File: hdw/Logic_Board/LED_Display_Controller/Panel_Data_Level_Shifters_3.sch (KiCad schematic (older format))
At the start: 43 parts, among them U2801 74LVC1G32, U2802 74HCT541

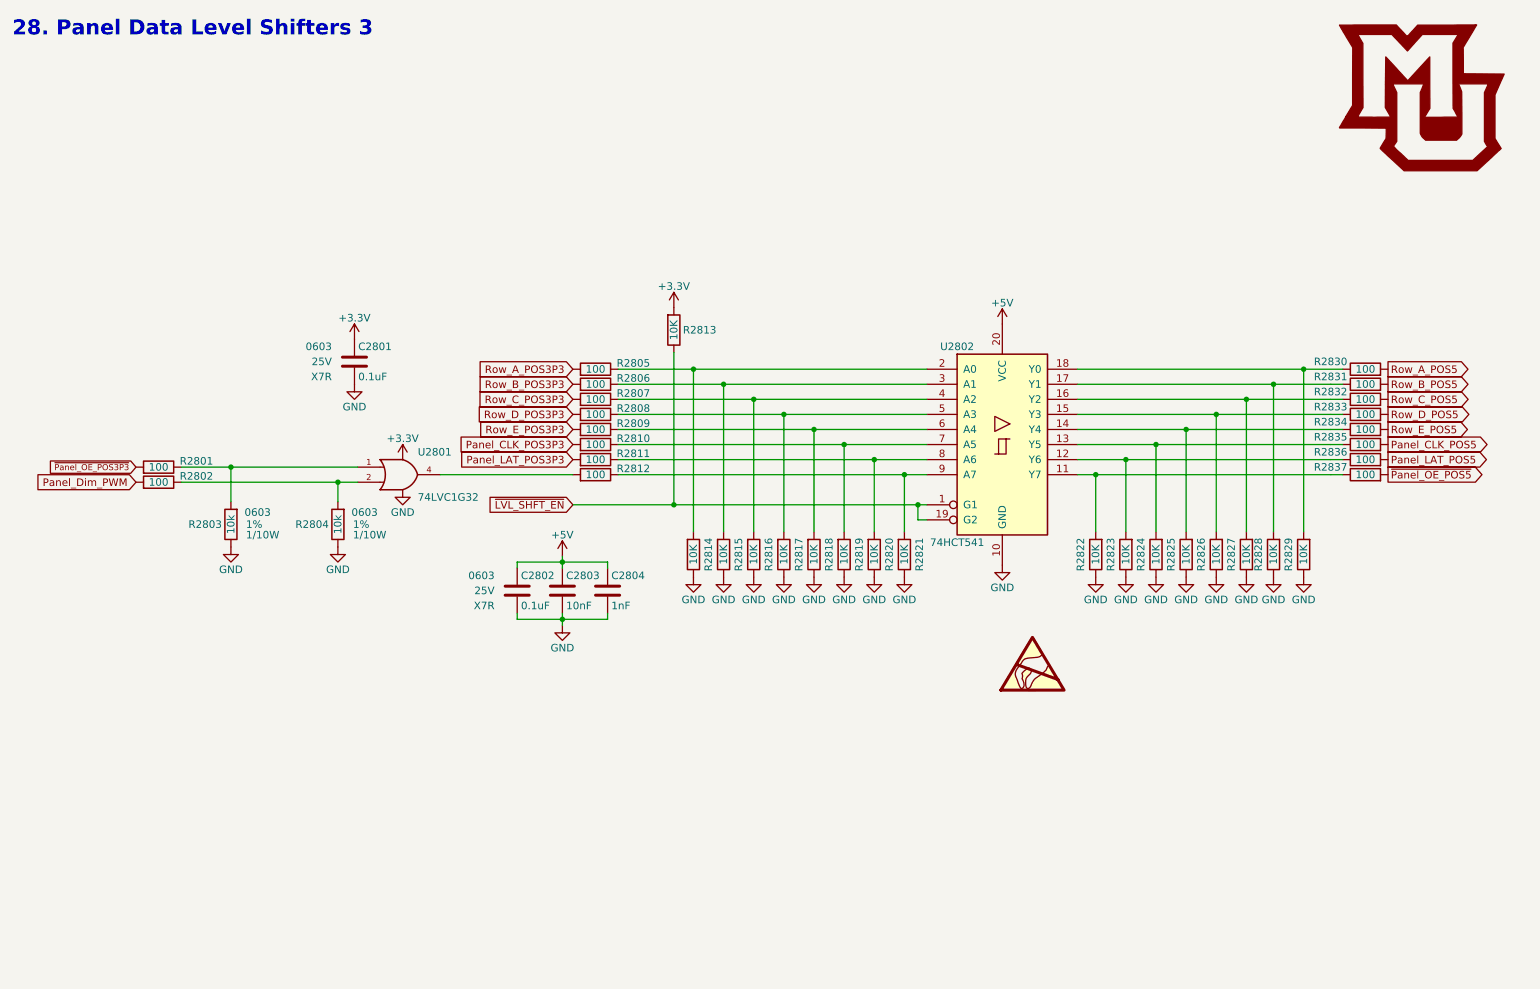
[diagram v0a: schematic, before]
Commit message: Changed a few pull resistors
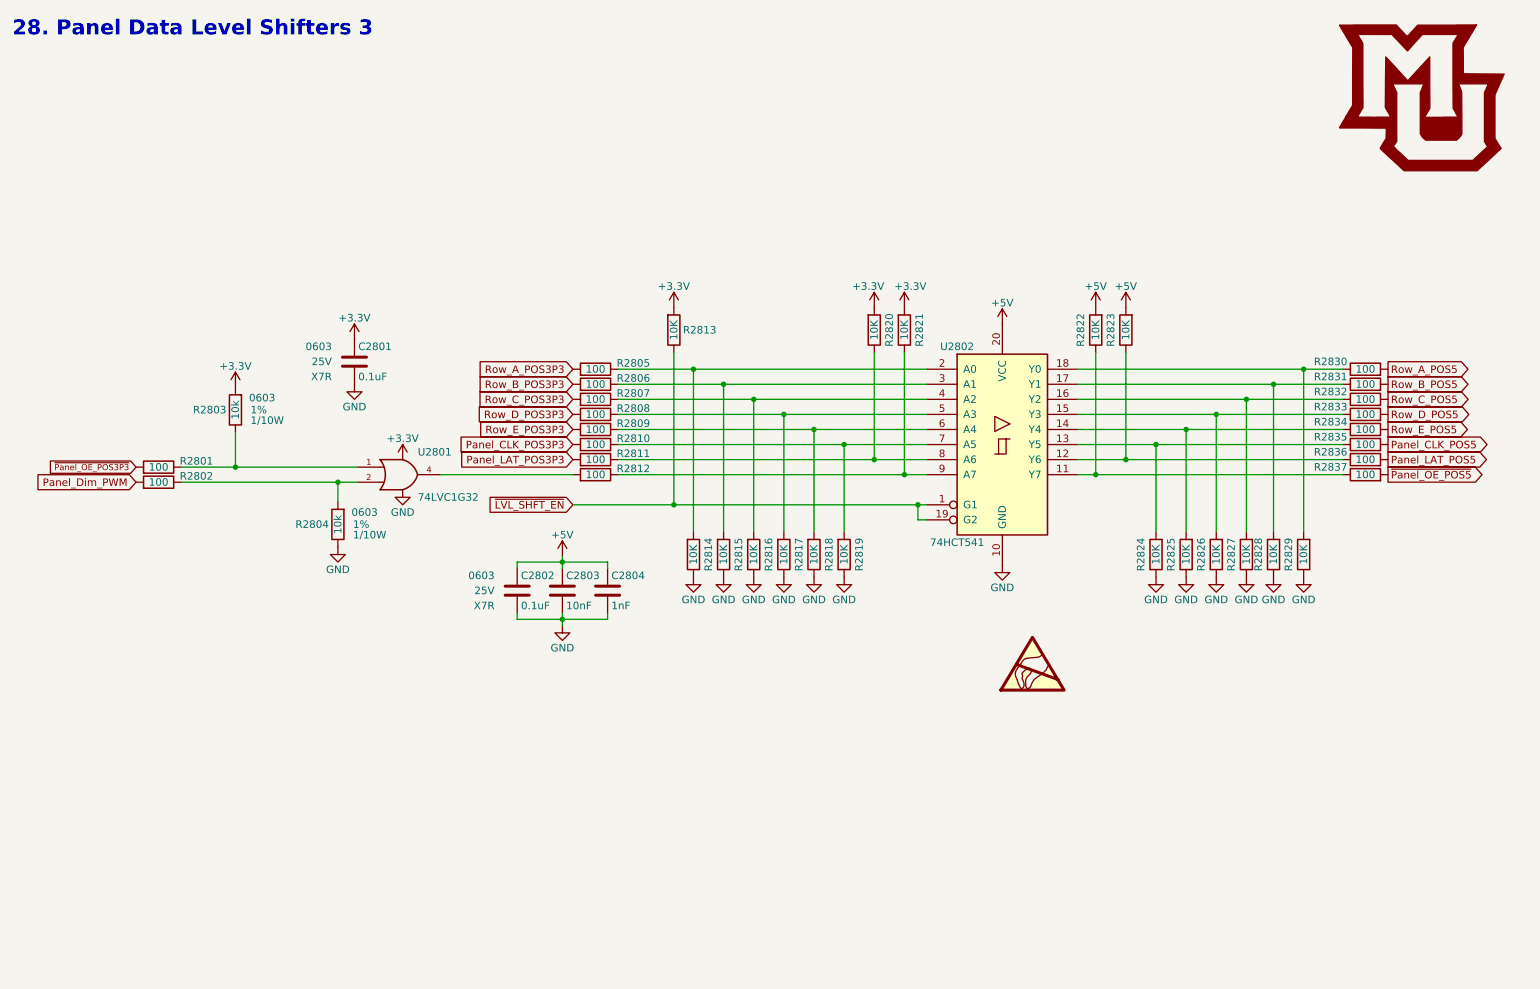
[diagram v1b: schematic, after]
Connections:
- net +3V3: now also R2803.1, R2820.1, R2821.1
- net +5V: now also R2822.1, R2823.1
- net GND: no longer R2803.2, R2820.2, R2821.2, R2822.2, R2823.2
- net at R2811.2, U2802.8 (A6): now also R2820.2; no longer R2820.1
- net at R2812.2, U2802.9 (A7): now also R2821.2; no longer R2821.1
- net at R2836.2, U2802.12 (Y6): now also R2823.2; no longer R2823.1
- net at R2837.2, U2802.11 (Y7): now also R2822.2; no longer R2822.1
- net at R2801.2, U2801.1: now also R2803.2; no longer R2803.1
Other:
- moved on the sheet: R2803, R2820, R2821, R2822, R2823

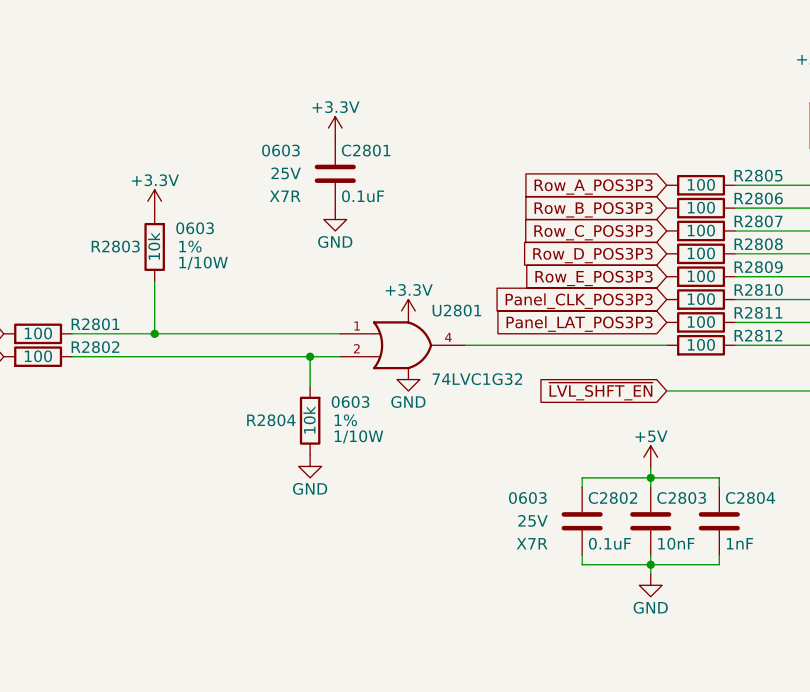
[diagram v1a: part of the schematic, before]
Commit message: Added some digikey partnumbers to components
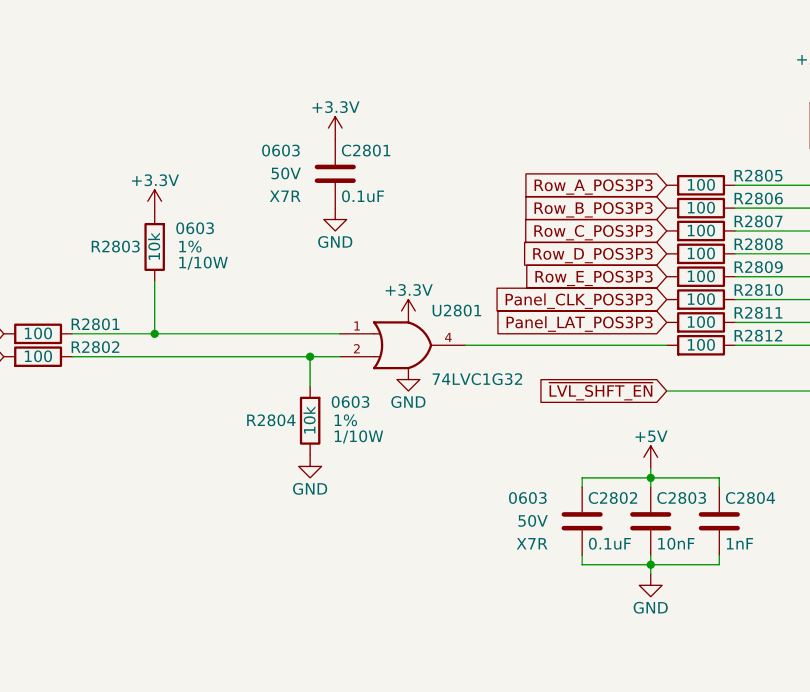
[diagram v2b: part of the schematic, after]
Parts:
- C2801, C2802: footprint (none) -> Capacitors_SMD:C_0603; Digi-Key PN PN -> 311-1344-1-ND; Voltage 25V -> 50V
- C2803: Digi-Key PN PN -> 1276-1921-1-ND; Voltage 25V -> 50V
- C2804: Digi-Key PN PN -> 1276-1018-1-ND; Voltage 25V -> 50V
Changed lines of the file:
@@
 F 0 "C2802" H 3925 4470 50  0000 L CNN
 F 1 "0.1uF" H 3925 4270 50  0000 L CNN
-F 2 "" H 3938 4220 50  0001 C CNN
+F 2 "Capacitors_SMD:C_0603" H 3938 4220 50  0001 C CNN
 F 3 "" H 3925 4470 50  0001 C CNN
 F 4 "0603" H 3750 4470 50  0000 R CNN "display_footprint"
-F 5 "25V" H 3750 4370 50  0000 R CNN "Voltage"
+F 5 "50V" H 3750 4370 50  0000 R CNN "Voltage"
 F 6 "X7R" H 3750 4270 50  0000 R CNN "Dielectric"
-F 7 "PN" H 4325 4870 60  0001 C CNN "Digi-Key PN"
+F 7 "311-1344-1-ND" H 4325 4870 60  0001 C CNN "Digi-Key PN"
 	1    3900 4370
 	1    0    0    -1
@@
 F 3 "" H 4225 4470 50  0001 C CNN
 F 4 "0603" H 4050 4470 50  0001 R CNN "display_footprint"
-F 5 "25V" H 4050 4370 50  0001 R CNN "Voltage"
+F 5 "50V" H 4050 4370 50  0001 R CNN "Voltage"
 F 6 "X7R" H 4050 4270 50  0001 R CNN "Dielectric"
-F 7 "PN" H 4625 4870 60  0001 C CNN "Digi-Key PN"
+F 7 "1276-1921-1-ND" H 4625 4870 60  0001 C CNN "Digi-Key PN"
 	1    4200 4370
 	1    0    0    -1
@@
 F 3 "" H 4525 4470 50  0001 C CNN
 F 4 "0603" H 4350 4470 50  0001 R CNN "display_footprint"
-F 5 "25V" H 4350 4370 50  0001 R CNN "Voltage"
+F 5 "50V" H 4350 4370 50  0001 R CNN "Voltage"
 F 6 "X7R" H 4350 4270 50  0001 R CNN "Dielectric"
-F 7 "PN" H 4925 4870 60  0001 C CNN "Digi-Key PN"
+F 7 "1276-1018-1-ND" H 4925 4870 60  0001 C CNN "Digi-Key PN"
 	1    4500 4370
 	1    0    0    -1
@@
 F 0 "C2801" H 2845 2950 50  0000 L CNN
 F 1 "0.1uF" H 2845 2750 50  0000 L CNN
-F 2 "" H 2858 2700 50  0001 C CNN
+F 2 "Capacitors_SMD:C_0603" H 2858 2700 50  0001 C CNN
 F 3 "" H 2845 2950 50  0001 C CNN
 F 4 "0603" H 2670 2950 50  0000 R CNN "display_footprint"
-F 5 "25V" H 2670 2850 50  0000 R CNN "Voltage"
+F 5 "50V" H 2670 2850 50  0000 R CNN "Voltage"
 F 6 "X7R" H 2670 2750 50  0000 R CNN "Dielectric"
-F 7 "PN" H 3245 3350 60  0001 C CNN "Digi-Key PN"
+F 7 "311-1344-1-ND" H 3245 3350 60  0001 C CNN "Digi-Key PN"
 	1    2820 2850
 	1    0    0    -1

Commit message: Finished first pass of digikey part numbers
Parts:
- R2801, R2802, R2805, R2806, R2807, R2808, R2809, R2810, R2811, R2812, R2830, R2831, R2832, R2833, R2834, R2835, R2836, R2837: Digi-Key PN PN -> A106047CT-ND
- R2803, R2804, R2813, R2814, R2815, R2816, R2817, R2818, R2819, R2820, R2821, R2822, R2823, R2824, R2825, R2826, R2827, R2828, R2829: Digi-Key PN PN -> RMCF0603FT10K0CT-ND
- U2802: Digi-Key PN (none) -> 296-26499-1-ND
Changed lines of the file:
@@
 F 2 "" H 7120 3400 50  0001 C CNN
 F 3 "http://www.ti.com/lit/gpn/sn74HCT541" H 7120 3400 50  0001 C CNN
+F 4 "296-26499-1-ND" H 0   0   50  0001 C CNN "Digi-Key PN"
 	1    7120 3400
 	1    0    0    -1
@@
 F 5 "1%" H 7810 2640 50  0001 L CNN "Tolerance"
 F 6 "1/10W" H 7810 2560 50  0001 L CNN "Wattage"
-F 7 "PN" H 8040 3040 60  0001 C CNN "Digi-Key PN"
+F 7 "RMCF0603FT10K0CT-ND" H 8040 3040 60  0001 C CNN "Digi-Key PN"
 	1    7740 2640
 	1    0    0    -1
@@
 F 5 "1%" H 8010 2640 50  0001 L CNN "Tolerance"
 F 6 "1/10W" H 8010 2560 50  0001 L CNN "Wattage"
-F 7 "PN" H 8240 3040 60  0001 C CNN "Digi-Key PN"
+F 7 "RMCF0603FT10K0CT-ND" H 8240 3040 60  0001 C CNN "Digi-Key PN"
 	1    7940 2640
 	1    0    0    -1
@@
 F 5 "1%" H 8210 4130 50  0001 L CNN "Tolerance"
 F 6 "1/10W" H 8210 4050 50  0001 L CNN "Wattage"
-F 7 "PN" H 8440 4530 60  0001 C CNN "Digi-Key PN"
+F 7 "RMCF0603FT10K0CT-ND" H 8440 4530 60  0001 C CNN "Digi-Key PN"
 	1    8140 4130
 	1    0    0    -1
@@
 F 5 "1%" H 8410 4130 50  0001 L CNN "Tolerance"
 F 6 "1/10W" H 8410 4050 50  0001 L CNN "Wattage"
-F 7 "PN" H 8640 4530 60  0001 C CNN "Digi-Key PN"
+F 7 "RMCF0603FT10K0CT-ND" H 8640 4530 60  0001 C CNN "Digi-Key PN"
 	1    8340 4130
 	1    0    0    -1
@@
 F 5 "1%" H 8610 4130 50  0001 L CNN "Tolerance"
 F 6 "1/10W" H 8610 4050 50  0001 L CNN "Wattage"
-F 7 "PN" H 8840 4530 60  0001 C CNN "Digi-Key PN"
+F 7 "RMCF0603FT10K0CT-ND" H 8840 4530 60  0001 C CNN "Digi-Key PN"
 	1    8540 4130
 	1    0    0    -1
@@
 F 5 "1%" H 8810 4130 50  0001 L CNN "Tolerance"
 F 6 "1/10W" H 8810 4050 50  0001 L CNN "Wattage"
-F 7 "PN" H 9040 4530 60  0001 C CNN "Digi-Key PN"
+F 7 "RMCF0603FT10K0CT-ND" H 9040 4530 60  0001 C CNN "Digi-Key PN"
 	1    8740 4130
 	1    0    0    -1
@@
 F 5 "1%" V 9730 2900 50  0001 C CNN "Tolerance"
 F 6 "1/10W" V 9830 2900 50  0001 C CNN "Wattage"
-F 7 "PN" H 9830 3300 60  0001 C CNN "Digi-Key PN"
+F 7 "A106047CT-ND" H 9830 3300 60  0001 C CNN "Digi-Key PN"
 	1    9530 2900
 	0    1    1    0
@@
 F 5 "1%" H 6140 4130 50  0001 L CNN "Tolerance"
 F 6 "1/10W" H 6140 4050 50  0001 L CNN "Wattage"
-F 7 "PN" H 6370 4530 60  0001 C CNN "Digi-Key PN"
+F 7 "RMCF0603FT10K0CT-ND" H 6370 4530 60  0001 C CNN "Digi-Key PN"
 	1    6070 4130
 	-1   0    0    -1
@@
 F 5 "1%" H 5940 4130 50  0001 L CNN "Tolerance"
 F 6 "1/10W" H 5940 4050 50  0001 L CNN "Wattage"
-F 7 "PN" H 6170 4530 60  0001 C CNN "Digi-Key PN"
+F 7 "RMCF0603FT10K0CT-ND" H 6170 4530 60  0001 C CNN "Digi-Key PN"
 	1    5870 4130
 	-1   0    0    -1
@@
 F 5 "1%" H 5740 4130 50  0001 L CNN "Tolerance"
 F 6 "1/10W" H 5740 4050 50  0001 L CNN "Wattage"
-F 7 "PN" H 5970 4530 60  0001 C CNN "Digi-Key PN"
+F 7 "RMCF0603FT10K0CT-ND" H 5970 4530 60  0001 C CNN "Digi-Key PN"
 	1    5670 4130
 	-1   0    0    -1
@@
 F 5 "1%" H 5540 4130 50  0001 L CNN "Tolerance"
 F 6 "1/10W" H 5540 4050 50  0001 L CNN "Wattage"
-F 7 "PN" H 5770 4530 60  0001 C CNN "Digi-Key PN"
+F 7 "RMCF0603FT10K0CT-ND" H 5770 4530 60  0001 C CNN "Digi-Key PN"
 	1    5470 4130
 	-1   0    0    -1
@@
 F 5 "1%" H 5340 4130 50  0001 L CNN "Tolerance"
 F 6 "1/10W" H 5340 4050 50  0001 L CNN "Wattage"
-F 7 "PN" H 5570 4530 60  0001 C CNN "Digi-Key PN"
+F 7 "RMCF0603FT10K0CT-ND" H 5570 4530 60  0001 C CNN "Digi-Key PN"
 	1    5270 4130
 	-1   0    0    -1
@@
 F 5 "1%" H 5140 4130 50  0001 L CNN "Tolerance"
 F 6 "1/10W" H 5140 4050 50  0001 L CNN "Wattage"
-F 7 "PN" H 5370 4530 60  0001 C CNN "Digi-Key PN"
+F 7 "RMCF0603FT10K0CT-ND" H 5370 4530 60  0001 C CNN "Digi-Key PN"
 	1    5070 4130
 	-1   0    0    -1
@@
 F 5 "1%" V 4620 2900 50  0001 C CNN "Tolerance"
 F 6 "1/10W" V 4720 2900 50  0001 C CNN "Wattage"
-F 7 "PN" H 4720 3300 60  0001 C CNN "Digi-Key PN"
+F 7 "A106047CT-ND" H 4720 3300 60  0001 C CNN "Digi-Key PN"
 	1    4420 2900
 	0    -1   1    0
@@
 F 5 "1%" H 6340 2640 50  0001 L CNN "Tolerance"
 F 6 "1/10W" H 6340 2560 50  0001 L CNN "Wattage"
-F 7 "PN" H 6570 3040 60  0001 C CNN "Digi-Key PN"
+F 7 "RMCF0603FT10K0CT-ND" H 6570 3040 60  0001 C CNN "Digi-Key PN"
 	1    6270 2640
 	-1   0    0    -1
@@
 F 5 "1%" H 6540 2640 50  0001 L CNN "Tolerance"
 F 6 "1/10W" H 6540 2560 50  0001 L CNN "Wattage"
-F 7 "PN" H 6770 3040 60  0001 C CNN "Digi-Key PN"
+F 7 "RMCF0603FT10K0CT-ND" H 6770 3040 60  0001 C CNN "Digi-Key PN"
 	1    6470 2640
 	-1   0    0    -1
@@
 F 5 "1%" H 5010 2640 50  0001 L CNN "Tolerance"
 F 6 "1/10W" H 5010 2560 50  0001 L CNN "Wattage"
-F 7 "PN" H 5240 3040 60  0001 C CNN "Digi-Key PN"
+F 7 "RMCF0603FT10K0CT-ND" H 5240 3040 60  0001 C CNN "Digi-Key PN"
 	1    4940 2640
 	-1   0    0    -1
@@
 F 5 "1%" V 4620 3000 50  0001 C CNN "Tolerance"
 F 6 "1/10W" V 4720 3000 50  0001 C CNN "Wattage"
-F 7 "PN" H 4720 3400 60  0001 C CNN "Digi-Key PN"
+F 7 "A106047CT-ND" H 4720 3400 60  0001 C CNN "Digi-Key PN"
 	1    4420 3000
 	0    -1   1    0
@@
 F 5 "1%" V 4620 3100 50  0001 C CNN "Tolerance"
 F 6 "1/10W" V 4720 3100 50  0001 C CNN "Wattage"
-F 7 "PN" H 4720 3500 60  0001 C CNN "Digi-Key PN"
+F 7 "A106047CT-ND" H 4720 3500 60  0001 C CNN "Digi-Key PN"
 	1    4420 3100
 	0    -1   1    0
@@
 F 5 "1%" V 4620 3200 50  0001 C CNN "Tolerance"
 F 6 "1/10W" V 4720 3200 50  0001 C CNN "Wattage"
-F 7 "PN" H 4720 3600 60  0001 C CNN "Digi-Key PN"
+F 7 "A106047CT-ND" H 4720 3600 60  0001 C CNN "Digi-Key PN"
 	1    4420 3200
 	0    -1   1    0
@@
 F 5 "1%" V 4620 3300 50  0001 C CNN "Tolerance"
 F 6 "1/10W" V 4720 3300 50  0001 C CNN "Wattage"
-F 7 "PN" H 4720 3700 60  0001 C CNN "Digi-Key PN"
+F 7 "A106047CT-ND" H 4720 3700 60  0001 C CNN "Digi-Key PN"
 	1    4420 3300
 	0    -1   1    0
@@
 F 5 "1%" V 4620 3400 50  0001 C CNN "Tolerance"
 F 6 "1/10W" V 4720 3400 50  0001 C CNN "Wattage"
-F 7 "PN" H 4720 3800 60  0001 C CNN "Digi-Key PN"
+F 7 "A106047CT-ND" H 4720 3800 60  0001 C CNN "Digi-Key PN"
 	1    4420 3400
 	0    -1   1    0
@@
 F 5 "1%" V 9730 3000 50  0001 C CNN "Tolerance"
 F 6 "1/10W" V 9830 3000 50  0001 C CNN "Wattage"
-F 7 "PN" H 9830 3400 60  0001 C CNN "Digi-Key PN"
+F 7 "A106047CT-ND" H 9830 3400 60  0001 C CNN "Digi-Key PN"
 	1    9530 3000
 	0    1    1    0
@@
 F 5 "1%" V 9730 3100 50  0001 C CNN "Tolerance"
 F 6 "1/10W" V 9830 3100 50  0001 C CNN "Wattage"
-F 7 "PN" H 9830 3500 60  0001 C CNN "Digi-Key PN"
+F 7 "A106047CT-ND" H 9830 3500 60  0001 C CNN "Digi-Key PN"
 	1    9530 3100
 	0    1    1    0
@@
 F 5 "1%" V 9730 3200 50  0001 C CNN "Tolerance"
 F 6 "1/10W" V 9830 3200 50  0001 C CNN "Wattage"
-F 7 "PN" H 9830 3600 60  0001 C CNN "Digi-Key PN"
+F 7 "A106047CT-ND" H 9830 3600 60  0001 C CNN "Digi-Key PN"
 	1    9530 3200
 	0    1    1    0
@@
 F 5 "1%" V 9730 3300 50  0001 C CNN "Tolerance"
 F 6 "1/10W" V 9830 3300 50  0001 C CNN "Wattage"
-F 7 "PN" H 9830 3700 60  0001 C CNN "Digi-Key PN"
+F 7 "A106047CT-ND" H 9830 3700 60  0001 C CNN "Digi-Key PN"
 	1    9530 3300
 	0    1    1    0
@@
 F 5 "1%" V 9730 3400 50  0001 C CNN "Tolerance"
 F 6 "1/10W" V 9830 3400 50  0001 C CNN "Wattage"
-F 7 "PN" H 9830 3800 60  0001 C CNN "Digi-Key PN"
+F 7 "A106047CT-ND" H 9830 3800 60  0001 C CNN "Digi-Key PN"
 	1    9530 3400
 	0    1    1    0
@@
 F 5 "1%" V 4620 3500 50  0001 C CNN "Tolerance"
 F 6 "1/10W" V 4720 3500 50  0001 C CNN "Wattage"
-F 7 "PN" H 4720 3900 60  0001 C CNN "Digi-Key PN"
+F 7 "A106047CT-ND" H 4720 3900 60  0001 C CNN "Digi-Key PN"
 	1    4420 3500
 	0    -1   1    0
@@
 F 5 "1%" V 4620 3600 50  0001 C CNN "Tolerance"
 F 6 "1/10W" V 4720 3600 50  0001 C CNN "Wattage"
-F 7 "PN" H 4720 4000 60  0001 C CNN "Digi-Key PN"
+F 7 "A106047CT-ND" H 4720 4000 60  0001 C CNN "Digi-Key PN"
 	1    4420 3600
 	0    -1   1    0
@@
 F 5 "1%" V 9730 3500 50  0001 C CNN "Tolerance"
 F 6 "1/10W" V 9830 3500 50  0001 C CNN "Wattage"
-F 7 "PN" H 9830 3900 60  0001 C CNN "Digi-Key PN"
+F 7 "A106047CT-ND" H 9830 3900 60  0001 C CNN "Digi-Key PN"
 	1    9530 3500
 	0    1    1    0
@@
 F 5 "1%" V 9730 3600 50  0001 C CNN "Tolerance"
 F 6 "1/10W" V 9830 3600 50  0001 C CNN "Wattage"
-F 7 "PN" H 9830 4000 60  0001 C CNN "Digi-Key PN"
+F 7 "A106047CT-ND" H 9830 4000 60  0001 C CNN "Digi-Key PN"
 	1    9530 3600
 	0    1    1    0
@@
 F 5 "1%" H 8990 4130 50  0001 L CNN "Tolerance"
 F 6 "1/10W" H 8990 4050 50  0001 L CNN "Wattage"
-F 7 "PN" H 9220 4530 60  0001 C CNN "Digi-Key PN"
+F 7 "RMCF0603FT10K0CT-ND" H 9220 4530 60  0001 C CNN "Digi-Key PN"
 	1    8920 4130
 	1    0    0    -1
@@
 F 5 "1%" H 9190 4130 50  0001 L CNN "Tolerance"
 F 6 "1/10W" H 9190 4050 50  0001 L CNN "Wattage"
-F 7 "PN" H 9420 4530 60  0001 C CNN "Digi-Key PN"
+F 7 "RMCF0603FT10K0CT-ND" H 9420 4530 60  0001 C CNN "Digi-Key PN"
 	1    9120 4130
 	1    0    0    -1
@@
 F 5 "1%" H 2810 3930 50  0000 L CNN "Tolerance"
 F 6 "1/10W" H 2810 3860 50  0000 L CNN "Wattage"
-F 7 "PN" H 3010 4330 60  0001 C CNN "Digi-Key PN"
+F 7 "RMCF0603FT10K0CT-ND" H 3010 4330 60  0001 C CNN "Digi-Key PN"
 	1    2710 3930
 	1    0    0    -1
@@
 F 5 "1%" H 2130 3170 50  0000 L CNN "Tolerance"
 F 6 "1/10W" H 2130 3100 50  0000 L CNN "Wattage"
-F 7 "PN" H 2330 3570 60  0001 C CNN "Digi-Key PN"
+F 7 "RMCF0603FT10K0CT-ND" H 2330 3570 60  0001 C CNN "Digi-Key PN"
 	1    2030 3170
 	1    0    0    -1
@@
 F 5 "1%" V 1720 3550 50  0001 C CNN "Tolerance"
 F 6 "1/10W" V 1820 3550 50  0001 C CNN "Wattage"
-F 7 "PN" H 1820 3950 60  0001 C CNN "Digi-Key PN"
+F 7 "A106047CT-ND" H 1820 3950 60  0001 C CNN "Digi-Key PN"
 	1    1520 3550
 	0    -1   1    0
@@
 F 5 "1%" V 1720 3650 50  0001 C CNN "Tolerance"
 F 6 "1/10W" V 1820 3650 50  0001 C CNN "Wattage"
-F 7 "PN" H 1820 4050 60  0001 C CNN "Digi-Key PN"
+F 7 "A106047CT-ND" H 1820 4050 60  0001 C CNN "Digi-Key PN"
 	1    1520 3650
 	0    -1   1    0

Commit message: First pass assignment of footprints to all components
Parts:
- C2803, C2804: footprint (none) -> Capacitors_SMD:C_0603
- R2801, R2802, R2803, R2804, R2805, R2806, R2807, R2808, R2809, R2810, R2811, R2812, R2813, R2814, R2815, R2816, R2817, R2818, R2819, R2820, R2821, R2822, R2823, R2824, R2825, R2826, R2827, R2828, R2829, R2830, R2831, R2832, R2833, R2834, R2835, R2836, R2837: footprint (none) -> Resistors_SMD:R_0603
- U2802: footprint (none) -> Housings_SSOP:TSSOP-20_4.4x6.5mm_Pitch0.65mm
